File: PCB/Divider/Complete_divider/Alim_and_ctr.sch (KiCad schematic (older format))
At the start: 43 parts

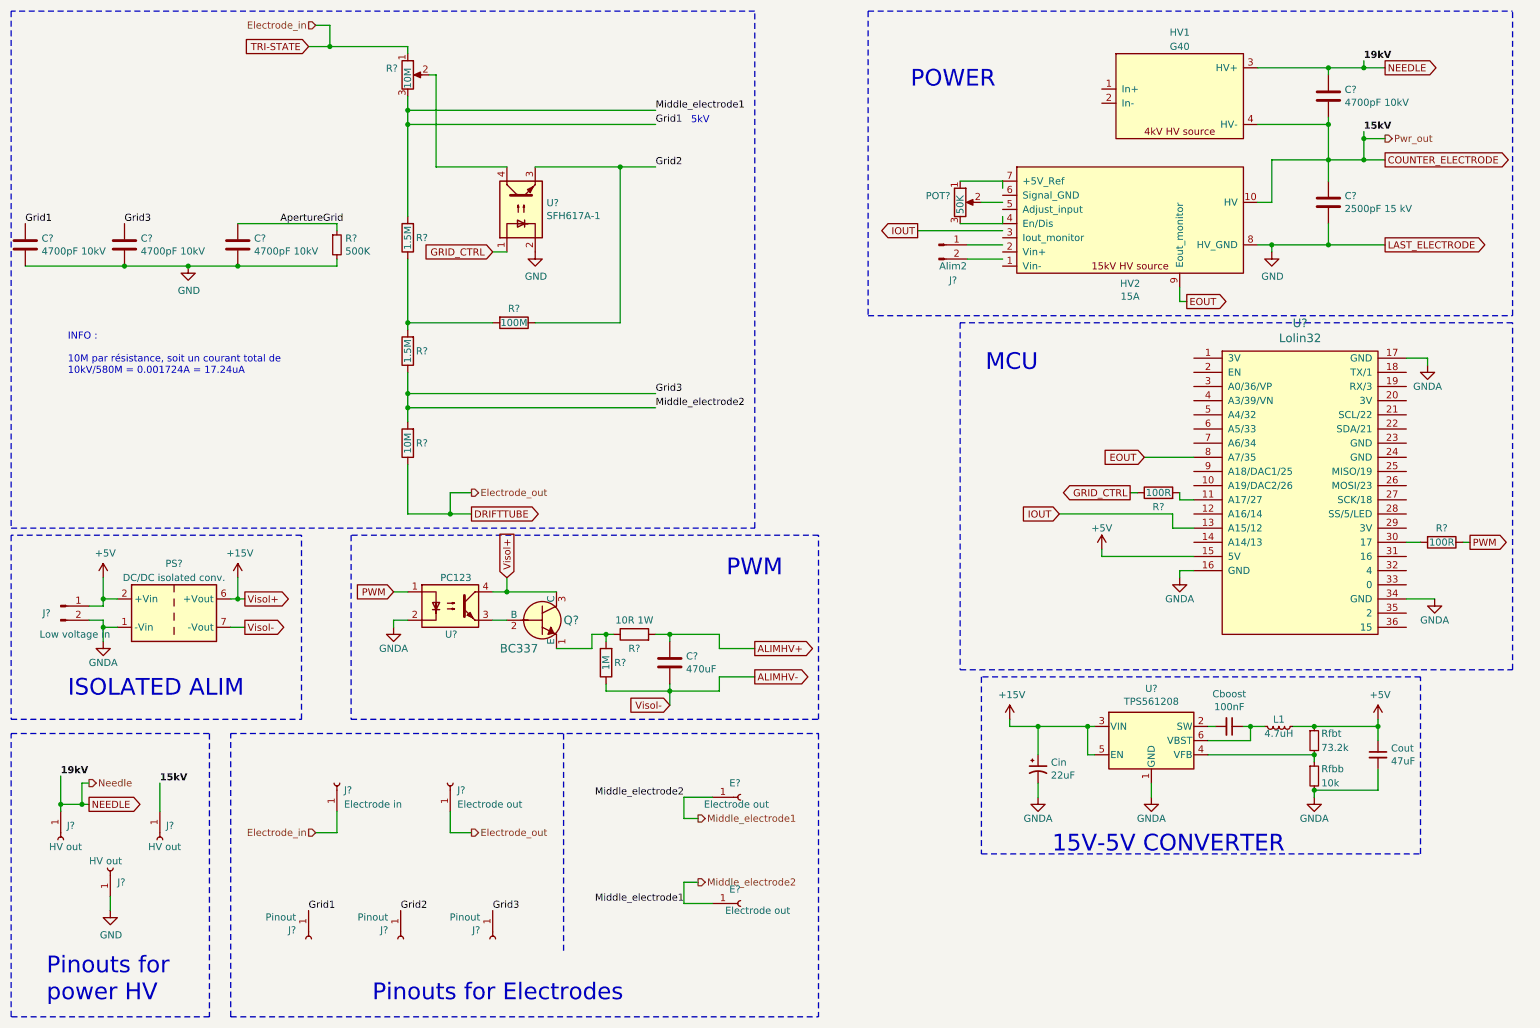
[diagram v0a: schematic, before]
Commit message: Set a Vin of 5V
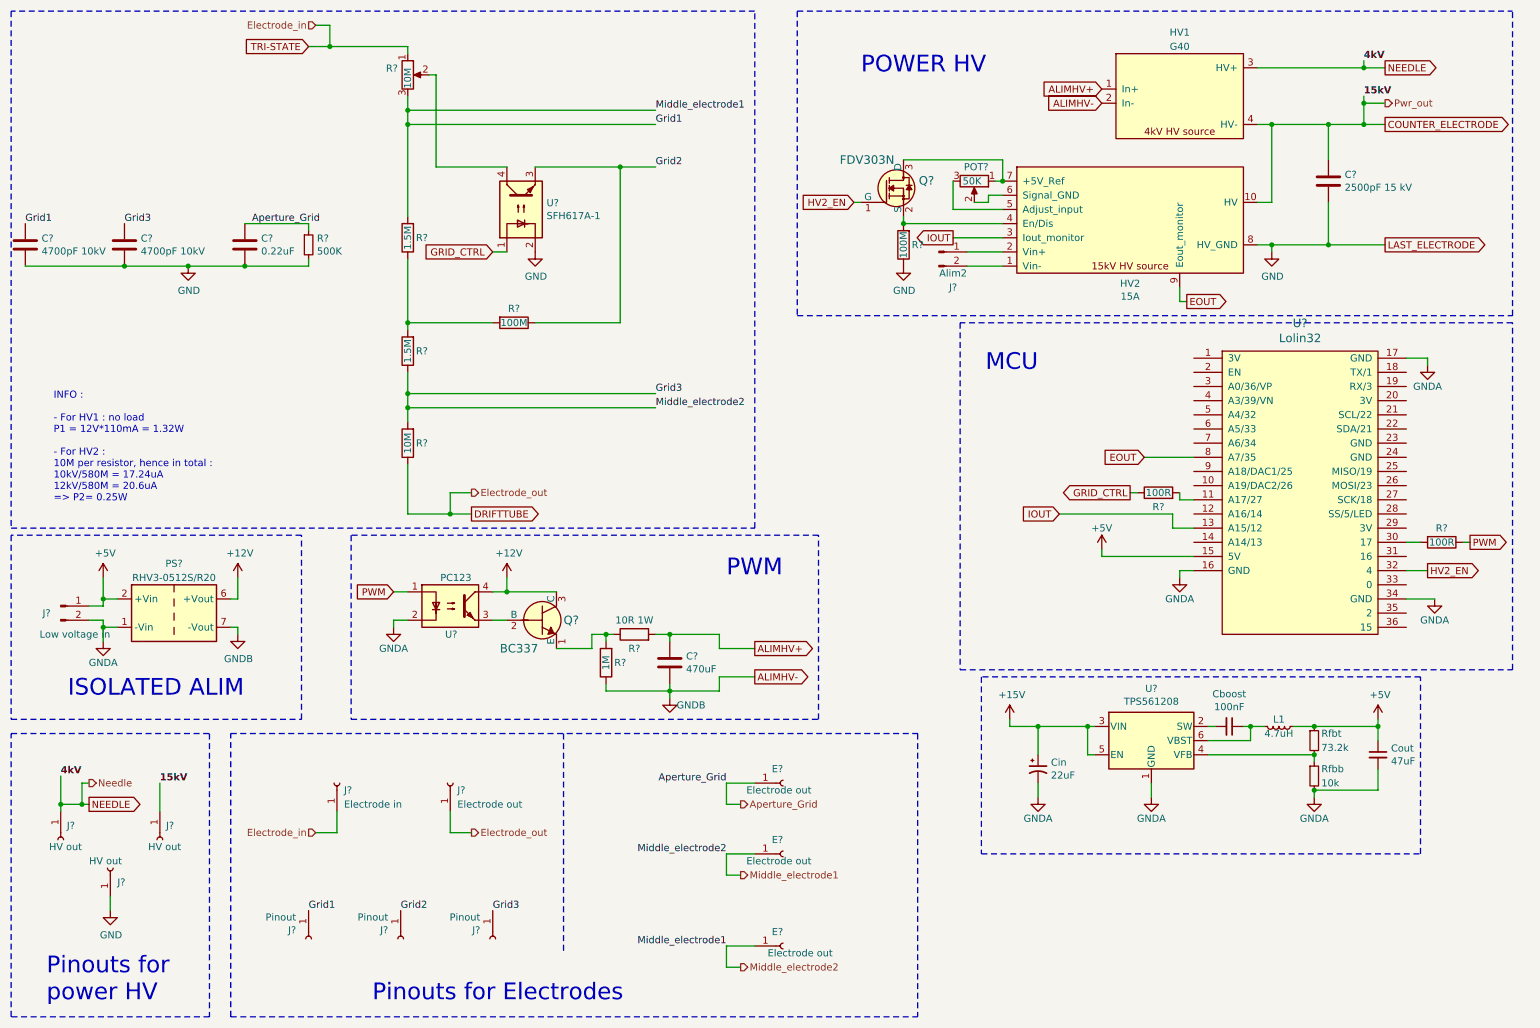
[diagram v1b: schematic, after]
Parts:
- removed C?: 4700pF 10kV, Capacitor_THT:C_Rect_L13.0mm_W8.0mm_P10.00mm_FKS3_FKP3_MKS4, symbol Device:C
- added E?: Electrode out, Connector_Pin:Pin_D1.0mm_L10.0mm, symbol Connector:Conn_01x01_Female
- added Q?: FDV303N, digikey-footprints:SOT-23-3, symbol dk_Transistors-FETs-MOSFETs-Single:FDV303N
- added R?: 100M, symbol Device:R
- C?: value 4700pF 10kV -> 0.22uF
- PS?: value DC/DC isolated conv. -> RHV3-0512S/R20
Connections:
- net labels added: +12V, 4kV, Aperture_Grid, GNDB, HV2_EN
- net labels removed: 19kV, ApertureGrid, Visol+, Visol-
- wire segments 163 -> 169
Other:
- note added: "INFO : \n\n- For HV1 : no load \nP1 = 12V*110mA = 1.32W\n\n- For HV2 : \n10M per resistor, hence in total : \n10kV/580M = 17.24uA\n12kV/580M = 20.6uA \n=> P2= 0.25W\n\n"
- note added: "POWER HV"
- note removed: "15V-5V CONVERTER\n"
- note removed: "5kV"
- note removed: "INFO : \n\n10M par résistance, soit un courant total de \n10kV/580M = 0.001724A = 17.24uA\n\n"
- note removed: "POWER"
- moved on the sheet: C?, E?, J?, POT?, R?

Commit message: Small changes
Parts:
- removed Cboost: 100nF, symbol Device:C_Small
- removed Cin: 22uF, symbol Device:CP1_Small
- removed Cout: 47uF, symbol Device:C_Small
- removed L1: 4.7uH, symbol Device:L_Small
- removed Rfbb: 10k, Resistor_SMD:R_1206_3216Metric, symbol Device:R_Small
- removed Rfbt: 73.2k, Resistor_SMD:R_1206_3216Metric, symbol Device:R_Small
- removed U?: TPS561208, Package_TO_SOT_SMD:SOT-23-6, symbol Regulator_Switching:TPS562200
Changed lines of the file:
@@
 	10550 3000 10400 3000
-$Comp
-L Regulator_Switching:TPS562200 U?
-U 1 1 5EA52D20
-P 8600 5700
-F 0 "U?" H 8600 6067 50  0000 C CNN
-F 1 "TPS561208" H 8600 5976 50  0000 C CNN
-F 2 "Package_TO_SOT_SMD:SOT-23-6" H 8650 5450 50  0001 L CNN
-F 3 "http://www.ti.com/lit/ds/symlink/tps563200.pdf" H 8600 5700 50  0001 C CNN
-	1    8600 5700
-	1    0    0    -1
-$EndComp
-Wire Wire Line
-	7800 5800 7800 5600
-Wire Wire Line
-	8200 5800 8150 5800
-Wire Wire Line
-	8150 5800 8150 5600
-Connection ~ 8150 5600
-Wire Wire Line
-	8150 5600 8200 5600
-$Comp
-L power:+15V #PWR?
-U 1 1 5EA9D284
-P 7600 5550
-F 0 "#PWR?" H 7600 5400 50  0001 C CNN
-F 1 "+15V" H 7615 5723 50  0000 C CNN
-F 2 "" H 7600 5550 50  0001 C CNN
-F 3 "" H 7600 5550 50  0001 C CNN
-	1    7600 5550
-	1    0    0    -1
-$EndComp
-Wire Wire Line
-	7600 5550 7600 5600
-$Comp
-L Device:C_Small Cboost
-U 1 1 5EABD013
-P 9150 5600
-F 0 "Cboost" V 8921 5600 50  0000 C CNN
-F 1 "100nF" V 9012 5600 50  0000 C CNN
-F 2 "" H 9150 5600 50  0001 C CNN
-F 3 "~" H 9150 5600 50  0001 C CNN
-	1    9150 5600
-	0    1    1    0
-$EndComp
-$Comp
-L Device:L_Small L1
-U 1 1 5EACACD4
-P 9500 5600
-F 0 "L1" V 9450 5600 50  0000 C CNN
-F 1 "4.7uH" V 9550 5600 50  0000 C CNN
-F 2 "" H 9500 5600 50  0001 C CNN
-F 3 "~" H 9500 5600 50  0001 C CNN
-	1    9500 5600
-	0    1    1    0
-$EndComp
-$Comp
-L Device:R_Small Rfbt
-U 1 1 5EAE71C6
-P 9750 5700
-F 0 "Rfbt" H 9800 5750 50  0000 L CNN
-F 1 "73.2k" H 9800 5650 50  0000 L CNN
-F 2 "Resistor_SMD:R_1206_3216Metric" H 9750 5700 50  0001 C CNN
-F 3 "~" H 9750 5700 50  0001 C CNN
-	1    9750 5700
-	1    0    0    -1
-$EndComp
-$Comp
-L Device:R_Small Rfbb
-U 1 1 5EB02F4B
-P 9750 5950
-F 0 "Rfbb" H 9800 6000 50  0000 L CNN
-F 1 "10k" H 9800 5900 50  0000 L CNN
-F 2 "Resistor_SMD:R_1206_3216Metric" H 9750 5950 50  0001 C CNN
-F 3 "~" H 9750 5950 50  0001 C CNN
-	1    9750 5950
-	1    0    0    -1
-$EndComp
-Wire Wire Line
-	9600 5600 9750 5600
-Wire Wire Line
-	9750 5850 9750 5800
-Connection ~ 9750 5800
-$Comp
-L Device:C_Small Cout
-U 1 1 5EB208ED
-P 10200 5800
-F 0 "Cout" H 10292 5846 50  0000 L CNN
-F 1 "47uF" H 10292 5755 50  0000 L CNN
-F 2 "" H 10200 5800 50  0001 C CNN
-F 3 "~" H 10200 5800 50  0001 C CNN
-	1    10200 5800
-	1    0    0    -1
-$EndComp
-Wire Wire Line
-	10200 5700 10200 5600
-Wire Wire Line
-	10200 5600 9750 5600
-Connection ~ 9750 5600
-Wire Wire Line
-	9750 6050 10200 6050
-Wire Wire Line
-	10200 6050 10200 5900
-Wire Wire Line
-	9050 5600 9000 5600
-Wire Wire Line
-	9300 5600 9300 5700
-Wire Wire Line
-	9300 5700 9000 5700
-Wire Wire Line
-	9000 5800 9750 5800
-Wire Wire Line
-	9300 5600 9400 5600
-Wire Wire Line
-	9250 5600 9300 5600
-Connection ~ 9300 5600
-Wire Wire Line
-	7600 5600 7800 5600
-$Comp
-L Device:CP1_Small Cin
-U 1 1 5EB883F8
-P 7800 5900
-F 0 "Cin" H 7891 5946 50  0000 L CNN
-F 1 "22uF" H 7891 5855 50  0000 L CNN
-F 2 "" H 7800 5900 50  0001 C CNN
-F 3 "~" H 7800 5900 50  0001 C CNN
-	1    7800 5900
-	1    0    0    -1
-$EndComp
-Connection ~ 7800 5600
-Wire Wire Line
-	7800 5600 8150 5600
 $Comp
 L Device:R R?
@@
 	0    1    1    0
 $EndComp
-$Comp
-L power:+5V #PWR?
-U 1 1 5E8F6A23
-P 10200 5550
-F 0 "#PWR?" H 10200 5400 50  0001 C CNN
-F 1 "+5V" H 10215 5723 50  0000 C CNN
-F 2 "" H 10200 5550 50  0001 C CNN
-F 3 "" H 10200 5550 50  0001 C CNN
-	1    10200 5550
-	1    0    0    -1
-$EndComp
-Wire Wire Line
-	10200 5550 10200 5600
-Connection ~ 10200 5600
 $Comp
 L power:+5V #PWR?
@@
 	1    0    0    -1
 $EndComp
-$Comp
-L power:GNDA #PWR?
-U 1 1 5E98CF21
-P 9750 6100
-F 0 "#PWR?" H 9750 5850 50  0001 C CNN
-F 1 "GNDA" H 9750 5950 50  0000 C CNN
-F 2 "" H 9750 6100 50  0001 C CNN
-F 3 "" H 9750 6100 50  0001 C CNN
-	1    9750 6100
-	1    0    0    -1
-$EndComp
-Wire Wire Line
-	9750 6100 9750 6050
-Connection ~ 9750 6050
-$Comp
-L power:GNDA #PWR?
-U 1 1 5E9945EB
-P 8600 6100
-F 0 "#PWR?" H 8600 5850 50  0001 C CNN
-F 1 "GNDA" H 8600 5950 50  0000 C CNN
-F 2 "" H 8600 6100 50  0001 C CNN
-F 3 "" H 8600 6100 50  0001 C CNN
-	1    8600 6100
-	1    0    0    -1
-$EndComp
-Wire Wire Line
-	8600 6000 8600 6100
-$Comp
-L power:GNDA #PWR?
-U 1 1 5E99BB27
-P 7800 6100
-F 0 "#PWR?" H 7800 5850 50  0001 C CNN
-F 1 "GNDA" H 7800 5950 50  0000 C CNN
-F 2 "" H 7800 6100 50  0001 C CNN
-F 3 "" H 7800 6100 50  0001 C CNN
-	1    7800 6100
-	1    0    0    -1
-$EndComp
-Wire Wire Line
-	7800 6000 7800 6100
 $Comp
 L power:GNDA #PWR?
@@
 	4400 5050 4650 5050
 Wire Notes Line
-	7400 5250 7400 6500
-Wire Notes Line
-	7400 6500 10500 6500
-Wire Notes Line
-	10500 6500 10500 5250
-Wire Notes Line
-	10500 5250 7400 5250
-Wire Notes Line
 	6250 4250 2950 4250
